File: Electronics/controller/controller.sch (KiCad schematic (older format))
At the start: 23 parts, among them P1 POWER, P2 PANEL_1, P3 PANEL_2, P4 DIAL, P5 SWITCH, P6 LED_DISPLAY, Q1 BUZ11, U1 LM317T, U2 74HC595, U3 Arduino_Pro_Micro

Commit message: Putting the display onto the board directly.
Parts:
- removed P6: LED_DISPLAY, Pin_Headers:Pin_Header_Straight_2x08, symbol DIL16
- added LED_DISPLAY1: ATA3492BW, Cylindric:4_Digit-7_Segment_LED-ATA3492BW, symbol ATA3492BW
- Q1: value BUZ11 -> FET
- R10: value 330 -> 33R
- R11: value 1k -> 33R
- R2: value 33R -> 1k
- R3: value 33R -> 330
- R4: value 33R -> 10k
- R9: value 10k -> 33R

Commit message: Reworking controller board.
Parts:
- removed P4: DIAL, Connect:bornier3, symbol CONN_3
- removed P5: SWITCH, Connect:bornier2, symbol CONN_2
- added ENC1: Encoder, Cylindric:ALPS_Encoder-EC12E2420404, symbol Encoder
- added SW1: SW_PUSH, Discret:SW_PUSH-12mm, symbol SW_PUSH
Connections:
- net labels added: A0
- wire segments 89 -> 87
- no-connect marks 13 -> 12
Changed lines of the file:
@@
 LIBS:transistors
 LIBS:conn
+LIBS:linear
+LIBS:regul
+LIBS:74xx
+LIBS:cmos4000
+LIBS:adc-dac
+LIBS:memory
+LIBS:xilinx
+LIBS:special
+LIBS:microcontrollers
+LIBS:dsp
+LIBS:microchip
+LIBS:analog_switches
+LIBS:motorola
+LIBS:texas
+LIBS:intel
+LIBS:audio
+LIBS:interface
+LIBS:digital-audio
+LIBS:philips
+LIBS:display
+LIBS:cypress
+LIBS:siliconi
+LIBS:opto
+LIBS:atmel
+LIBS:contrib
+LIBS:valves
+LIBS:borniers
+LIBS:cylindric
 LIBS:controller-cache
-LIBS:digit_board-cache
 EELAYER 25 0
 EELAYER END
@@
 D16
 $Comp
-L CONN_3 P4
-U 1 1 54886458
-P 6700 1350
-F 0 "P4" V 6650 1350 50  0000 C CNN
-F 1 "DIAL" V 6750 1350 40  0000 C CNN
-F 2 "Connect:bornier3" H 6700 1350 60  0001 C CNN
-F 3 "" H 6700 1350 60  0000 C CNN
-	1    6700 1350
-	1    0    0    -1
-$EndComp
-$Comp
 L GND #PWR03
 U 1 1 54886459
@@
 	1    0    0    -1
 $EndComp
-$Comp
-L CONN_2 P5
-U 1 1 54886464
-P 8050 1250
-F 0 "P5" V 8000 1250 40  0000 C CNN
-F 1 "SWITCH" V 8100 1250 40  0000 C CNN
-F 2 "Connect:bornier2" H 8050 1250 60  0001 C CNN
-F 3 "" H 8050 1250 60  0000 C CNN
-	1    8050 1250
-	1    0    0    1
-$EndComp
-Text Label 7600 900  2    60   ~ 0
-D10
+Text Label 7400 1150 2    60   ~ 0
+A0
 Text Notes 7150 750  0    60   ~ 0
 Switch Input
@@
 L GND #PWR010
 U 1 1 5488646A
-P 7450 1450
-F 0 "#PWR010" H 7450 1450 30  0001 C CNN
-F 1 "GND" H 7450 1380 30  0001 C CNN
-F 2 "" H 7450 1450 60  0000 C CNN
-F 3 "" H 7450 1450 60  0000 C CNN
-	1    7450 1450
+P 8100 1250
+F 0 "#PWR010" H 8100 1250 30  0001 C CNN
+F 1 "GND" H 8100 1180 30  0001 C CNN
+F 2 "" H 8100 1250 60  0000 C CNN
+F 3 "" H 8100 1250 60  0000 C CNN
+	1    8100 1250
 	1    0    0    -1
 $EndComp
@@
 $EndComp
 Text Label 1750 5150 2    60   ~ 0
-D7
+D10
 Text Label 1750 5250 2    60   ~ 0
-D8
+D16
 Text Label 1750 5050 2    60   ~ 0
-D6
+D14
 Text Label 1750 4950 2    60   ~ 0
-D5
+D15
 $Comp
 L Arduino_Pro_Micro U3
@@
 NoConn ~ 9100 1350
 NoConn ~ 9100 1450
-NoConn ~ 10300 1950
 NoConn ~ 10300 1850
 NoConn ~ 10300 1750
@@
 	3950 2250 3950 2350
 Wire Wire Line
-	5650 1800 6200 1800
-Wire Wire Line
-	6200 1800 6200 1450
-Wire Wire Line
-	5650 1350 6350 1350
+	5650 1800 6550 1800
+Wire Wire Line
+	5650 1350 6200 1350
 Wire Wire Line
 	1450 1400 1850 1400
@@
 	10950 2800 8450 2800
 Wire Wire Line
-	6200 1450 6350 1450
-Wire Wire Line
-	6350 1250 6200 1250
-Wire Wire Line
-	6200 1250 6200 900
-Wire Wire Line
-	6200 900  5650 900
+	5650 900  6550 900
 Wire Wire Line
 	5650 1350 5650 1400
@@
 Wire Notes Line
 	6850 1900 5350 1900
-Wire Wire Line
-	7700 1350 7450 1350
-Wire Wire Line
-	7700 1150 7600 1150
-Wire Wire Line
-	7600 1150 7600 900
 Wire Notes Line
 	7150 750  8250 750
@@
 Wire Wire Line
 	3200 3950 3350 3950
-Wire Wire Line
-	7450 1350 7450 1450
 Wire Wire Line
 	9100 1550 8950 1550
@@
 Wire Notes Line
 	800  5950 800  3000
+$Comp
+L Encoder ENC1
+U 1 1 5488F621
+P 6500 1350
+F 0 "ENC1" H 6375 1575 60  0000 C CNN
+F 1 "Encoder" H 6500 1475 60  0000 C CNN
+F 2 "Cylindric:ALPS_Encoder-EC12E2420404" H 6500 1400 60  0001 C CNN
+F 3 "" H 6500 1400 60  0000 C CNN
+	1    6500 1350
+	0    1    1    0
+$EndComp
+Wire Wire Line
+	6550 900  6550 950
+Wire Wire Line
+	6550 1800 6550 1750
+$Comp
+L SW_PUSH SW1
+U 1 1 54890306
+P 7700 1150
+F 0 "SW1" H 7850 1260 50  0000 C CNN
+F 1 "SW_PUSH" H 7700 1070 50  0000 C CNN
+F 2 "Discret:SW_PUSH-12mm" H 7700 1150 60  0001 C CNN
+F 3 "" H 7700 1150 60  0000 C CNN
+	1    7700 1150
+	1    0    0    -1
+$EndComp
+Wire Wire Line
+	7400 1150 7250 1150
+Wire Wire Line
+	8000 1150 8100 1150
+Wire Wire Line
+	8100 1150 8100 1250
+Wire Wire Line
+	10300 1950 10450 1950
+Text Label 10450 1950 0    60   ~ 0
+A0
 $EndSCHEMATC

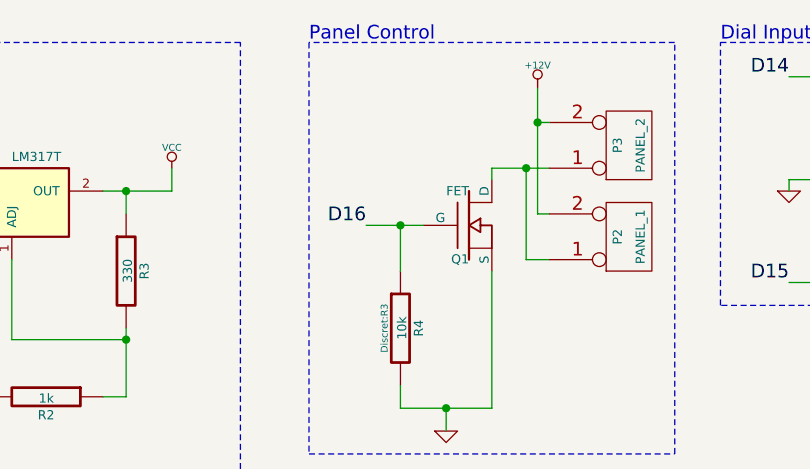
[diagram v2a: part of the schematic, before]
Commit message: Update with single layout board.
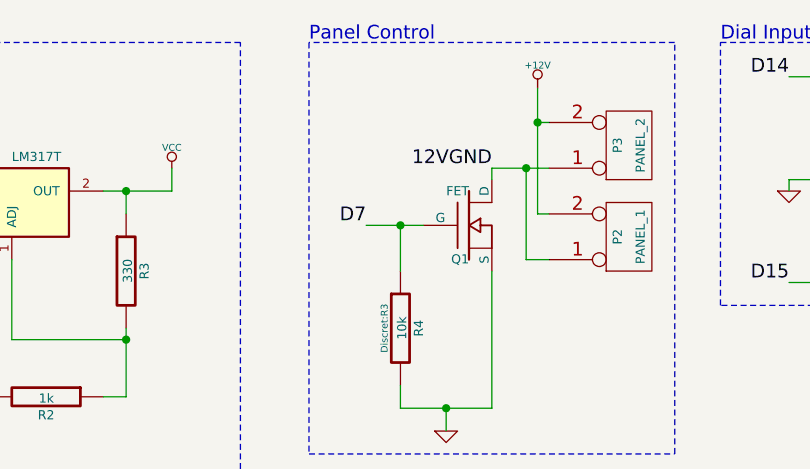
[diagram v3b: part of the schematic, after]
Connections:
- net D16: no longer Q1.G, R4.1
- net D7: now also Q1.G, R4.1
- net 12VGND: now reaches P2.1 (P1), P3.1 (P1), Q1.D
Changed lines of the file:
@@
 D15
 Text Label 3800 1550 2    60   ~ 0
-D16
+D7
 $Comp
 L GND #PWR03
@@
 Text Label 10450 1950 0    60   ~ 0
 A0
+Text Label 4350 1300 2    60   ~ 0
+12VGND
 $EndSCHEMATC

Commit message: Added missing file.
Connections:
- net COL: now also R1.1; no longer R1.2
- net D14: no longer C1.1, ENC1.A
- net D15: no longer C2.2, ENC1.B
- net D5: now also U3.8 (D5); no longer U3.11 (D8/A8)
- net D6: now also Q1.G, R4.1, U3.9 (D6/A7); no longer U3.10 (D7)
- net D7: now also U3.10 (D7); no longer Q1.G, R4.1, U3.9 (D6/A7)
- net D8: now also C2.2, ENC1.B, U3.11 (D8/A8); no longer U3.8 (D5)
- net at LED_DISPLAY1.4 (COL_AN): now also R1.2; no longer R1.1
- net D9: now reaches U3.12 (D9/A9)
- net D9: now also C1.1, ENC1.A
- no-connect marks 12 -> 11
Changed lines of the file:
@@
 D4
 Text Label 8950 1850 2    60   ~ 0
+D5
+Text Label 8950 1950 2    60   ~ 0
+D6
+Text Label 8950 2050 2    60   ~ 0
+D7
+Text Label 8950 2150 2    60   ~ 0
 D8
-Text Label 8950 1950 2    60   ~ 0
-D7
-Text Label 8950 2050 2    60   ~ 0
-D6
-Text Label 8950 2150 2    60   ~ 0
-D5
 Text Label 10450 2250 0    60   ~ 0
 D16
@@
 D15
 Text Label 3800 1550 2    60   ~ 0
-D7
+D6
 $Comp
 L GND #PWR03
@@
 $EndComp
 Text Label 5650 900  2    60   ~ 0
-D14
+D9
 Text Label 5650 1800 2    60   ~ 0
-D15
+D8
 $Comp
 L CONN_2 P1
@@
 F 3 "~" H 1650 5350 30  0000 C CNN
 	1    1650 5350
-	0    1    1    0
+	0    -1   -1   0
 $EndComp
 Text Label 1750 5150 2    60   ~ 0
@@
 Text Label 3350 3650 0    60   ~ 0
 COL
-NoConn ~ 9100 2250
 Wire Notes Line
 	10950 750  10950 2800
@@
 Text Label 4350 1300 2    60   ~ 0
 12VGND
+Wire Wire Line
+	9100 2250 8950 2250
+Text Label 8950 2250 2    60   ~ 0
+D9
 $EndSCHEMATC

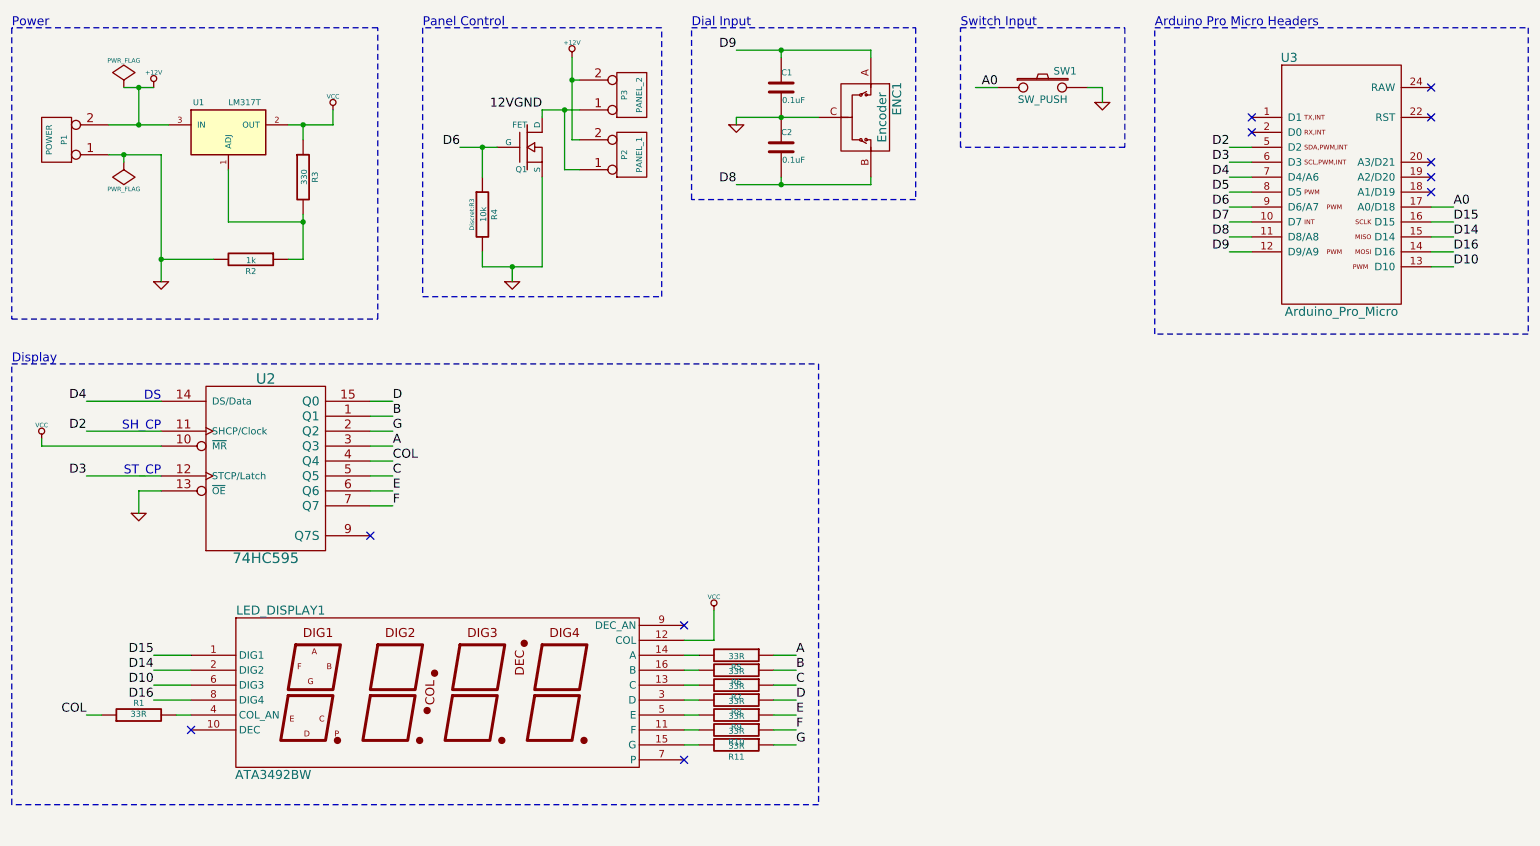
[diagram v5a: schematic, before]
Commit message: Change a couple of footprints.
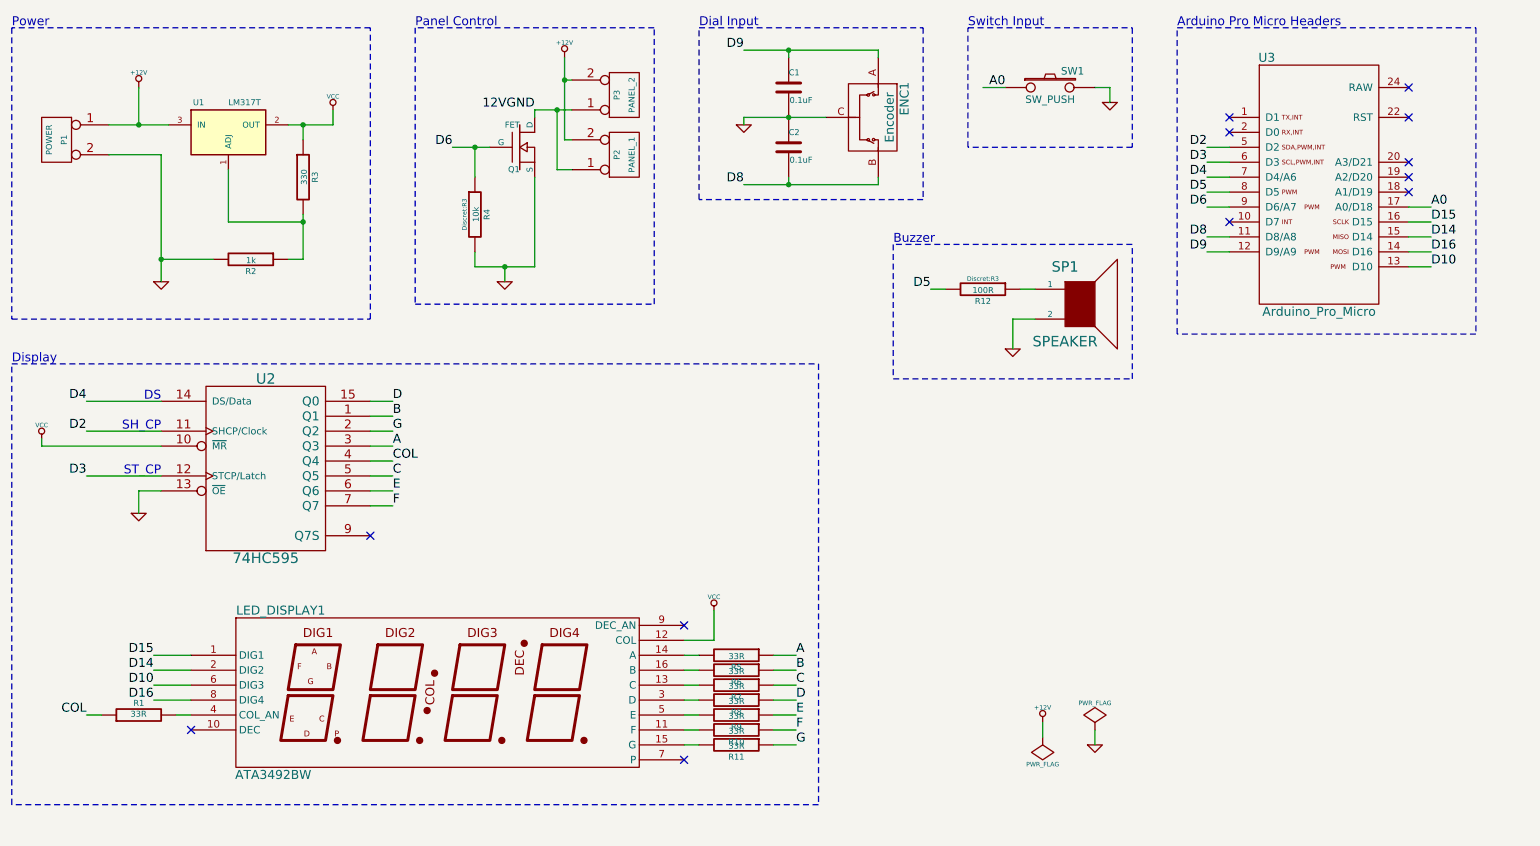
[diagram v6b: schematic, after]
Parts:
- added R12: 100R, Discret:R3, symbol R
- added SP1: SPEAKER, Pin_Headers:Pin_Header_Angled_1x02, symbol SPEAKER
- P1, P2, P3: footprint Connect:bornier2 -> Pin_Headers:Pin_Header_Angled_1x02
- U1: footprint Power_Integrations:TO-220 -> Transistors_TO-220:TO-220_Neutral123_Horizontal
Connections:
- net +12V: now also P1.1 (P1); no longer P1.2 (P2)
- net D5: now also R12.2
- net GND: now also P1.2 (P2), SP1.2; no longer P1.1 (P1)
- net D7: no longer names the net of U3.10 (D7)
- new net: R12.1, SP1.1
- no-connect marks 11 -> 12
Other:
- note added: "Buzzer"
- moved on the sheet: C1, C2, ENC1, P2, P3, Q1, R4, SW1, U3

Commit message: Fixed some bad pinouts on the 7-seg.
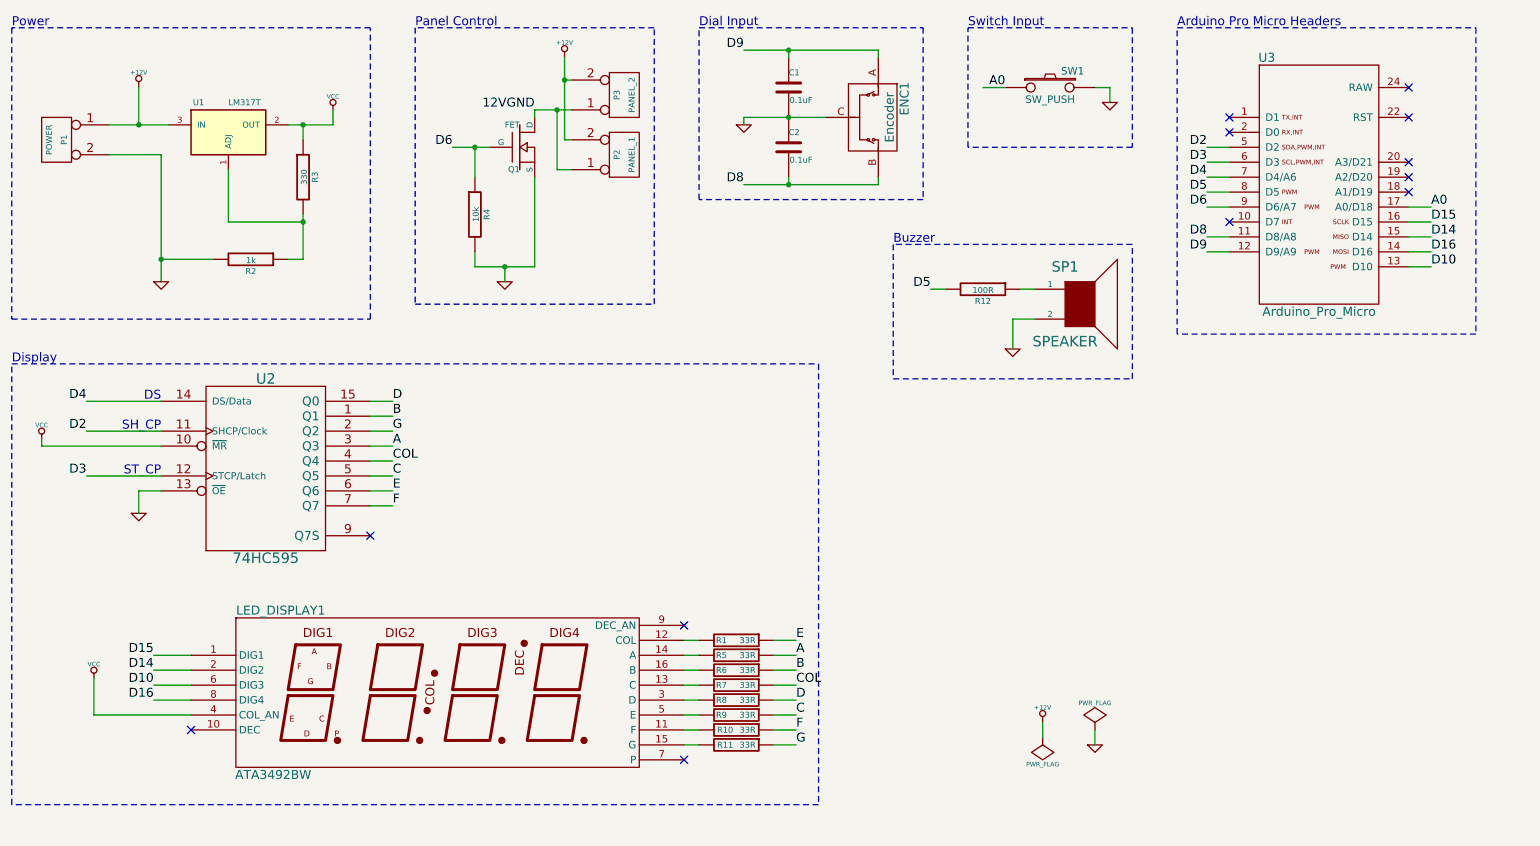
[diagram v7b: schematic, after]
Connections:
- net C: now also R9.1; no longer R7.1
- net COL: now also R7.1; no longer R1.1
- net E: now also R1.1; no longer R9.1
- net VCC: now also LED_DISPLAY1.4 (COL_AN); no longer LED_DISPLAY1.12 (COL)
- net at R1.2: now also LED_DISPLAY1.12 (COL); no longer LED_DISPLAY1.4 (COL_AN)
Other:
- moved on the sheet: R1
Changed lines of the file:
@@
 F 0 "R4" V 3980 2000 40  0000 C CNN
 F 1 "10k" V 3907 2001 40  0000 C CNN
-F 2 "Discret:R3" V 3830 2000 30  0000 C CNN
+F 2 "Discret:R3" V 3830 2000 30  0001 C CNN
 F 3 "~" H 3900 2000 30  0000 C CNN
 	1    3900 2000
@@
 U 1 1 54886468
 P 5650 5250
-F 0 "R8" V 5730 5250 40  0000 C CNN
-F 1 "33R" V 5657 5251 40  0000 C CNN
+F 0 "R8" V 5650 5150 40  0000 C CNN
+F 1 "33R" V 5650 5325 40  0000 C CNN
 F 2 "Discret:R3" V 5580 5250 30  0001 C CNN
 F 3 "~" H 5650 5250 30  0000 C CNN
@@
 U 1 1 54886469
 P 5650 5350
-F 0 "R9" V 5730 5350 40  0000 C CNN
-F 1 "33R" V 5657 5351 40  0000 C CNN
+F 0 "R9" V 5650 5250 40  0000 C CNN
+F 1 "33R" V 5650 5425 40  0000 C CNN
 F 2 "Discret:R3" V 5580 5350 30  0001 C CNN
 F 3 "~" H 5650 5350 30  0000 C CNN
@@
 U 1 1 5488646C
 P 5650 5050
-F 0 "R6" V 5730 5050 40  0000 C CNN
-F 1 "33R" V 5657 5051 40  0000 C CNN
+F 0 "R6" V 5650 4950 40  0000 C CNN
+F 1 "33R" V 5650 5125 40  0000 C CNN
 F 2 "Discret:R3" V 5580 5050 30  0001 C CNN
 F 3 "~" H 5650 5050 30  0000 C CNN
@@
 U 1 1 5488646D
 P 5650 5150
-F 0 "R7" V 5730 5150 40  0000 C CNN
-F 1 "33R" V 5657 5151 40  0000 C CNN
+F 0 "R7" V 5650 5050 40  0000 C CNN
+F 1 "33R" V 5650 5225 40  0000 C CNN
 F 2 "Discret:R3" V 5580 5150 30  0001 C CNN
 F 3 "~" H 5650 5150 30  0000 C CNN
@@
 U 1 1 5488646E
 P 5650 5450
-F 0 "R10" V 5730 5450 40  0000 C CNN
-F 1 "33R" V 5657 5451 40  0000 C CNN
+F 0 "R10" V 5650 5375 40  0000 C CNN
+F 1 "33R" V 5650 5525 40  0000 C CNN
 F 2 "Discret:R3" V 5580 5450 30  0001 C CNN
 F 3 "~" H 5650 5450 30  0000 C CNN
@@
 U 1 1 5488646F
 P 5650 5550
-F 0 "R11" V 5730 5550 40  0000 C CNN
-F 1 "33R" V 5657 5551 40  0000 C CNN
+F 0 "R11" V 5650 5475 40  0000 C CNN
+F 1 "33R" V 5650 5625 40  0000 C CNN
 F 2 "Discret:R3" V 5580 5550 30  0001 C CNN
 F 3 "~" H 5650 5550 30  0000 C CNN
@@
 U 1 1 54886470
 P 5650 4950
-F 0 "R5" V 5730 4950 40  0000 C CNN
-F 1 "33R" V 5657 4951 40  0000 C CNN
+F 0 "R5" V 5650 4850 40  0000 C CNN
+F 1 "33R" V 5650 5025 40  0000 C CNN
 F 2 "Discret:R3" V 5580 4950 30  0001 C CNN
 F 3 "~" H 5650 4950 30  0000 C CNN
@@
 L R R1
 U 1 1 54886471
-P 1650 5350
-F 0 "R1" V 1730 5350 40  0000 C CNN
-F 1 "33R" V 1657 5351 40  0000 C CNN
-F 2 "Discret:R3" V 1580 5350 30  0001 C CNN
-F 3 "~" H 1650 5350 30  0000 C CNN
-	1    1650 5350
-	0    -1   -1   0
+P 5650 4850
+F 0 "R1" V 5650 4750 40  0000 C CNN
+F 1 "33R" V 5650 4925 40  0000 C CNN
+F 2 "Discret:R3" V 5580 4850 30  0001 C CNN
+F 3 "~" H 5650 4850 30  0000 C CNN
+	1    5650 4850
+	0    1    1    0
 $EndComp
 Text Label 1750 5150 2    60   ~ 0
@@
 	4100 2350 4100 2450
 Wire Wire Line
-	3900 2350 4300 2350
+	3900 2350 4100 2350
+Wire Wire Line
+	4100 2350 4300 2350
 Wire Wire Line
 	4500 1500 4550 1500
@@
 	4450 1700 4550 1700
 Wire Wire Line
-	4500 950  4500 1500
+	4500 950  4500 1100
+Wire Wire Line
+	4500 1100 4500 1500
 Wire Wire Line
 	4500 1100 4550 1100
@@
 	3900 2250 3900 2350
 Wire Wire Line
-	5700 1800 6600 1800
-Wire Wire Line
-	5700 1350 6250 1350
-Wire Wire Line
-	1450 1400 1850 1400
+	5700 1800 6000 1800
+Wire Wire Line
+	6000 1800 6600 1800
+Wire Wire Line
+	5700 1350 6000 1350
+Wire Wire Line
+	6000 1350 6250 1350
+Wire Wire Line
+	1450 1400 1650 1400
+Wire Wire Line
+	1650 1400 1850 1400
 Connection ~ 1650 1400
 Wire Wire Line
 	1650 1400 1650 1150
 Wire Wire Line
-	2650 1400 2950 1400
+	2650 1400 2750 1400
+Wire Wire Line
+	2750 1400 2950 1400
 Wire Wire Line
 	2750 1400 2750 1500
@@
 	2250 2050 2750 2050
 Wire Wire Line
-	2750 2000 2750 2300
+	2750 2000 2750 2050
+Wire Wire Line
+	2750 2050 2750 2300
 Connection ~ 2750 2050
 Wire Wire Line
 	2150 2300 1800 2300
 Wire Wire Line
-	1800 1600 1800 2450
+	1800 1600 1800 2300
+Wire Wire Line
+	1800 2300 1800 2450
 Wire Wire Line
 	1450 1600 1800 1600
@@
 	10600 2800 8600 2800
 Wire Wire Line
-	5700 900  6600 900
+	5700 900  6000 900
+Wire Wire Line
+	6000 900  6600 900
 Wire Wire Line
 	5700 1350 5700 1400
@@
 	4300 1350 4300 1300
 Wire Wire Line
-	4300 1300 4550 1300
+	4300 1300 4450 1300
+Wire Wire Line
+	4450 1300 4550 1300
 Wire Wire Line
 	3900 1750 3900 1550
 Wire Wire Line
-	3750 1550 4000 1550
+	3750 1550 3900 1550
+Wire Wire Line
+	3900 1550 4000 1550
 Wire Wire Line
 	3200 3250 3350 3250
@@
 	1750 5250 2000 5250
 Wire Wire Line
-	1900 5350 2000 5350
-Wire Wire Line
-	5300 4850 5500 4850
+	1350 5350 2000 5350
+Wire Wire Line
+	5300 4850 5400 4850
 Wire Wire Line
 	5400 4950 5300 4950
@@
 Text Label 6050 5050 0    60   ~ 0
 B
-Text Label 6050 5150 0    60   ~ 0
+Text Label 6050 5350 0    60   ~ 0
 C
 Text Label 6050 5250 0    60   ~ 0
 D
-Text Label 6050 5350 0    60   ~ 0
+Text Label 6050 4850 0    60   ~ 0
 E
 Text Label 6050 5450 0    60   ~ 0
@@
 Text Label 6050 5550 0    60   ~ 0
 G
-Text Label 1300 5350 2    60   ~ 0
+Text Label 6050 5150 0    60   ~ 0
 COL
-Wire Wire Line
-	1400 5350 1300 5350
 Wire Wire Line
 	5900 4950 6050 4950
@@
 NoConn ~ 5300 4750
 NoConn ~ 2000 5450
-Wire Wire Line
-	5500 4850 5500 4650
 $Comp
 L VCC #PWR012
 U 1 1 54889554
-P 5500 4650
-F 0 "#PWR012" H 5500 4740 20  0001 C CNN
-F 1 "VCC" H 5500 4740 30  0000 C CNN
-F 2 "" H 5500 4650 60  0000 C CNN
-F 3 "" H 5500 4650 60  0000 C CNN
-	1    5500 4650
+P 1350 5100
+F 0 "#PWR012" H 1350 5190 20  0001 C CNN
+F 1 "VCC" H 1350 5190 30  0000 C CNN
+F 2 "" H 1350 5100 60  0000 C CNN
+F 3 "" H 1350 5100 60  0000 C CNN
+	1    1350 5100
 	1    0    0    -1
 $EndComp
@@
 F 0 "R12" V 7380 2500 40  0000 C CNN
 F 1 "100R" V 7307 2501 40  0000 C CNN
-F 2 "Discret:R3" V 7230 2500 30  0000 C CNN
+F 2 "Discret:R3" V 7230 2500 30  0001 C CNN
 F 3 "~" H 7300 2500 30  0000 C CNN
 	1    7300 2500
@@
 Text Notes 6700 2200 0    60   ~ 0
 Buzzer
+Wire Wire Line
+	5900 4850 6050 4850
+Wire Wire Line
+	1350 5350 1350 5100
 $EndSCHEMATC
